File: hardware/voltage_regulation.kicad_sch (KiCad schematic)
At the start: 33 parts, among them U4 TPS51388VABR, U5 LD39050PU33R

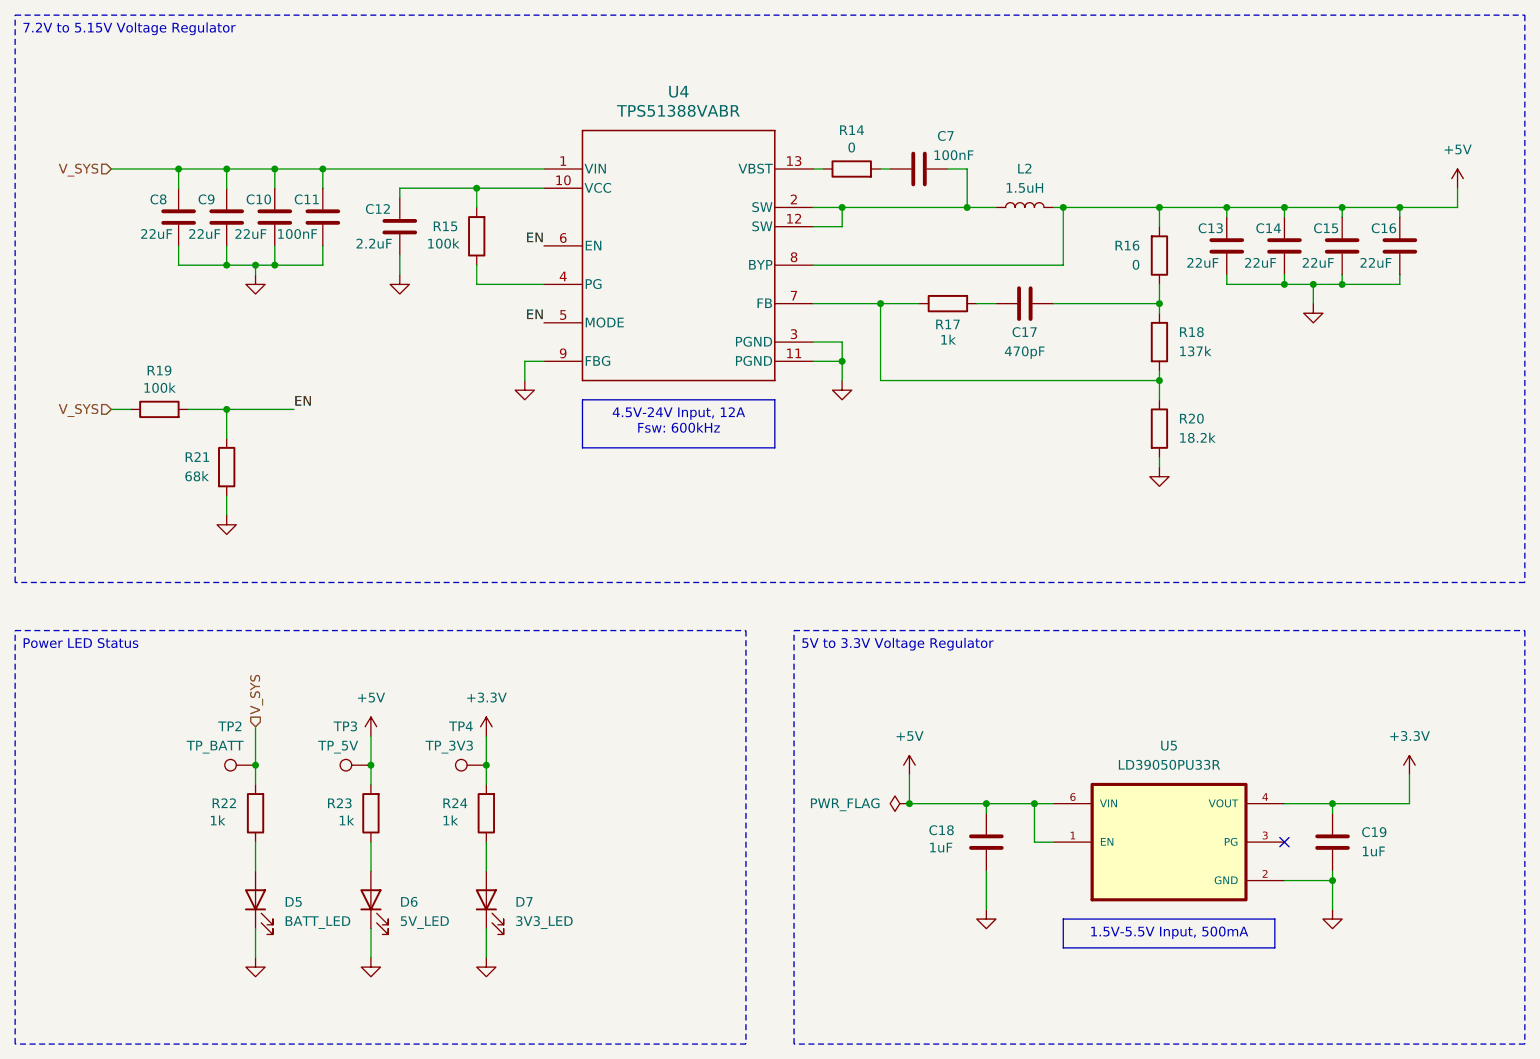
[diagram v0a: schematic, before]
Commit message: schematic update
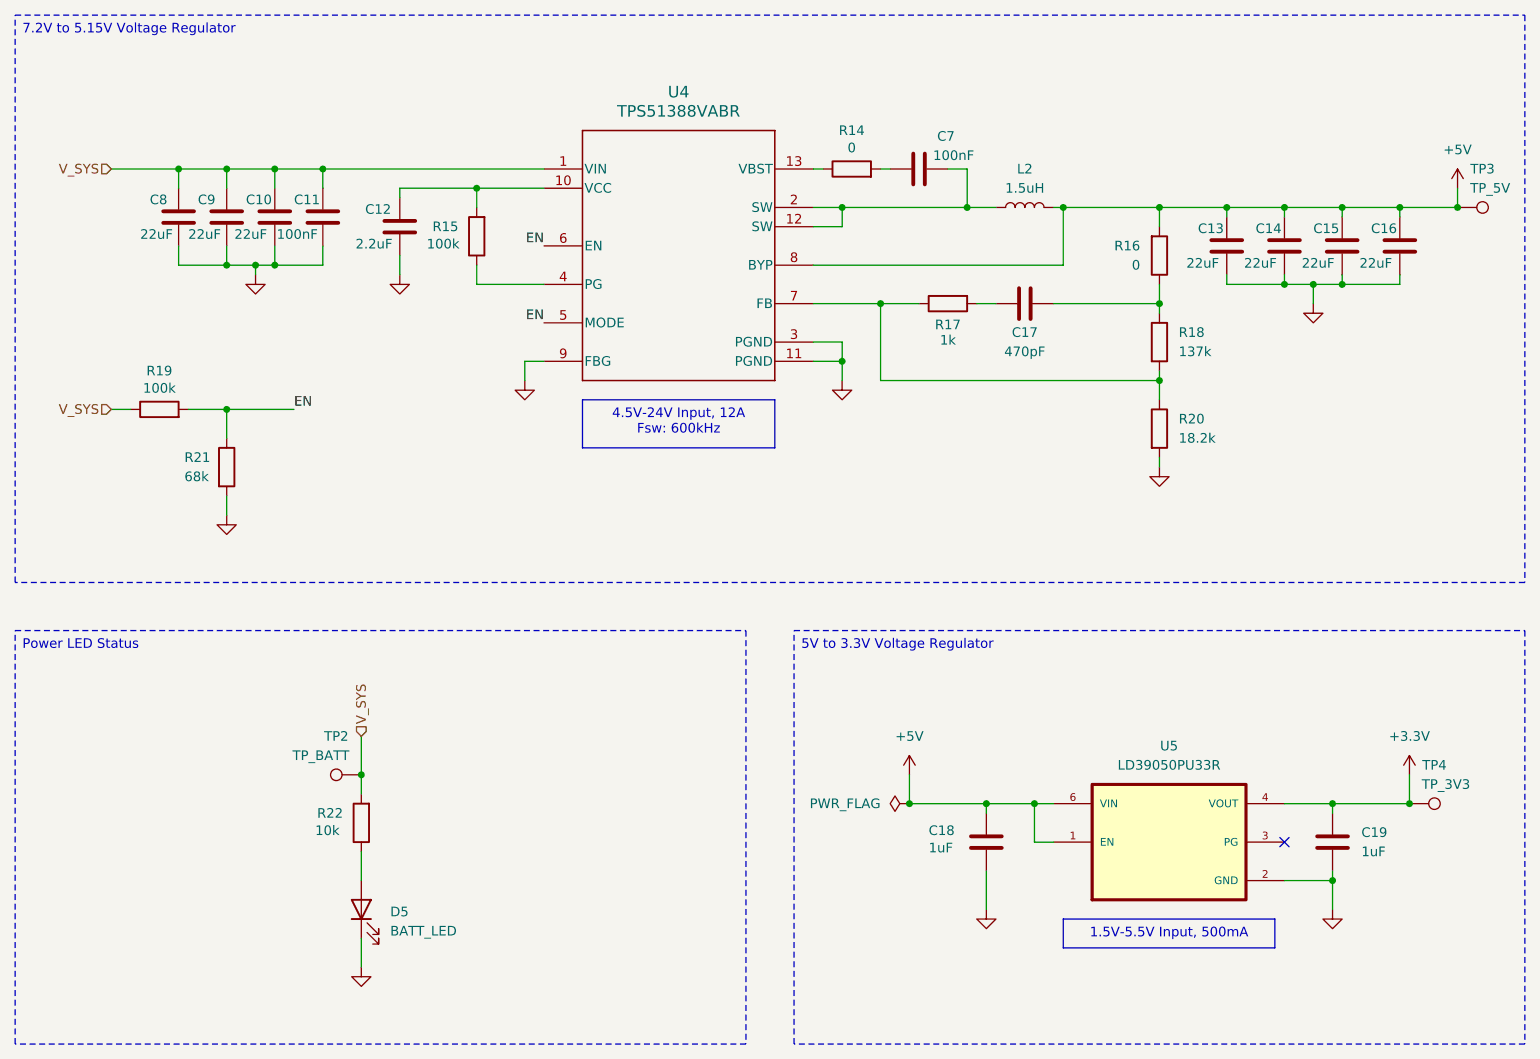
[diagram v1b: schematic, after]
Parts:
- removed D6: 5V_LED, LED_SMD:LED_0603_1608Metric, symbol Device:LED
- removed D7: 3V3_LED, LED_SMD:LED_0603_1608Metric, symbol Device:LED
- removed R23, R24: 1k, Resistor_SMD:R_0603_1608Metric, symbol Device:R
- D5: JLCPCB Part # C5478395 -> C6650185; MPN 150060SS55040 -> 150060BS55040
- R22: value 1k -> 10k; footprint Resistor_SMD:R_0603_1608Metric -> Resistor_SMD:R_0402_1005Metric; JLCPCB Part # (none) -> C191984
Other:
- moved on the sheet: D5, R22, TP2

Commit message: replacing components
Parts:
- D5: value BATT_LED -> 3V3 LED
- R22: value 10k -> 1k; JLCPCB Part # C191984 -> C844135
- renumbered TP3 to TP2, TP2 to TP3
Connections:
- net +3.3V: now also R22.2, TP3.1
- net V_SYS: no longer R22.2, TP3.1
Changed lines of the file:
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@@
 	(hierarchical_label "V_SYS"
 		(shape input)
-		(at 95.25 118.11 90)
-		(effects
-			(font
-				(size 1.27 1.27)
-			)
-			(justify left)
-		)
-	)
-	(hierarchical_label "V_SYS"
-		(shape input)
 		(at 62.23 43.18 180)
 		(effects
@@
 		(dnp no)
 		(fields_autoplaced yes)
-		(property "Reference" "#PWR030"
+		(property "Reference" "#PWR028"
 			(at 95.25 154.94 0)
 			(hide yes)
@@
 			(project "chromapi_motherboard_v1"
 				(path "/d1a31f26-03e0-43e1-89c1-031fe31befc5/19a2634a-eca3-4c2c-b35f-9c69362f2888"
-					(reference "#PWR030")
+					(reference "#PWR028")
 					(unit 1)
 				)
@@
 		(dnp no)
 		(fields_autoplaced yes)
-		(property "Reference" "#PWR028"
+		(property "Reference" "#PWR026"
 			(at 177.8 147.32 0)
 			(hide yes)
@@
 			(project "chromapi_motherboard_v1"
 				(path "/d1a31f26-03e0-43e1-89c1-031fe31befc5/19a2634a-eca3-4c2c-b35f-9c69362f2888"
-					(reference "#PWR028")
+					(reference "#PWR026")
 					(unit 1)
 				)
@@
 		(dnp no)
 		(fields_autoplaced yes)
-		(property "Reference" "#PWR029"
+		(property "Reference" "#PWR027"
 			(at 223.52 147.32 0)
 			(hide yes)
@@
 			(project "chromapi_motherboard_v1"
 				(path "/d1a31f26-03e0-43e1-89c1-031fe31befc5/19a2634a-eca3-4c2c-b35f-9c69362f2888"
-					(reference "#PWR029")
+					(reference "#PWR027")
 					(unit 1)
 				)
@@
 			)
 		)
-		(property "Value" "10k"
+		(property "Value" "1k"
 			(at 89.154 130.556 0)
 			(show_name no)
@@
 			)
 		)
-		(property "JLCPCB Part #" "C191984"
+		(property "JLCPCB Part #" "C844135"
 			(at 95.25 129.54 0)
 			(hide yes)
@@
 	)
 	(symbol
+		(lib_id "power:+3.3V")
+		(at 95.25 118.11 0)
+		(unit 1)
+		(body_style 1)
+		(exclude_from_sim no)
+		(in_bom yes)
+		(on_board yes)
+		(in_pos_files yes)
+		(dnp no)
+		(fields_autoplaced yes)
+		(property "Reference" "#PWR0112"
+			(at 95.25 121.92 0)
+			(hide yes)
+			(show_name no)
+			(do_not_autoplace no)
+			(effects
+				(font
+					(size 1.27 1.27)
+				)
+			)
+		)
+		(property "Value" "+3.3V"
+			(at 95.25 113.03 0)
+			(show_name no)
+			(do_not_autoplace no)
+			(effects
+				(font
+					(size 1.27 1.27)
+				)
+			)
+		)
+		(property "Footprint" ""
+			(at 95.25 118.11 0)
+			(hide yes)
+			(show_name no)
+			(do_not_autoplace no)
+			(effects
+				(font
+					(size 1.27 1.27)
+				)
+			)
+		)
+		(property "Datasheet" ""
+			(at 95.25 118.11 0)
+			(hide yes)
+			(show_name no)
+			(do_not_autoplace no)
+			(effects
+				(font
+					(size 1.27 1.27)
+				)
+			)
+		)
+		(property "Description" "Power symbol creates a global label with name \"+3.3V\""
+			(at 95.25 118.11 0)
+			(hide yes)
+			(show_name no)
+			(do_not_autoplace no)
+			(effects
+				(font
+					(size 1.27 1.27)
+				)
+			)
+		)
+		(pin "1"
+		)
+		(instances
+			(project "chromapi_motherboard_v1"
+				(path "/d1a31f26-03e0-43e1-89c1-031fe31befc5/19a2634a-eca3-4c2c-b35f-9c69362f2888"
+					(reference "#PWR0112")
+					(unit 1)
+				)
+			)
+		)
+	)
+	(symbol
 		(lib_id "Device:R")
 		(at 200.66 54.61 0)
@@
 		(in_pos_files yes)
 		(dnp no)
-		(property "Reference" "TP2"
+		(property "Reference" "TP3"
 			(at 91.948 118.11 90)
 			(show_name no)
@@
 			(project "chromapi_motherboard_v1"
 				(path "/d1a31f26-03e0-43e1-89c1-031fe31befc5/19a2634a-eca3-4c2c-b35f-9c69362f2888"
-					(reference "TP2")
+					(reference "TP3")
 					(unit 1)
 				)
@@
 		(dnp no)
 		(fields_autoplaced yes)
-		(property "Reference" "#PWR027"
+		(property "Reference" "#PWR025"
 			(at 233.68 127 0)
 			(hide yes)
@@
 			(project "chromapi_motherboard_v1"
 				(path "/d1a31f26-03e0-43e1-89c1-031fe31befc5/19a2634a-eca3-4c2c-b35f-9c69362f2888"
-					(reference "#PWR027")
+					(reference "#PWR025")
 					(unit 1)
 				)
@@
 		(in_pos_files yes)
 		(dnp no)
-		(property "Reference" "TP3"
+		(property "Reference" "TP2"
 			(at 243.332 43.18 90)
 			(show_name no)
@@
 			(project "chromapi_motherboard_v1"
 				(path "/d1a31f26-03e0-43e1-89c1-031fe31befc5/19a2634a-eca3-4c2c-b35f-9c69362f2888"
-					(reference "TP3")
+					(reference "TP2")
 					(unit 1)
 				)
@@
 		(dnp no)
 		(fields_autoplaced yes)
-		(property "Reference" "#PWR026"
+		(property "Reference" "#PWR024"
 			(at 167.64 127 0)
 			(hide yes)
@@
 			(project "chromapi_motherboard_v1"
 				(path "/d1a31f26-03e0-43e1-89c1-031fe31befc5/19a2634a-eca3-4c2c-b35f-9c69362f2888"
-					(reference "#PWR026")
+					(reference "#PWR024")
 					(unit 1)
 				)
@@
 			)
 		)
-		(property "Value" "BATT_LED"
+		(property "Value" "3V3 LED"
 			(at 99.06 143.8274 90)
 			(show_name no)

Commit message: schematic update
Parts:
- removed TP3: TP_BATT, TestPoint:TestPoint_Pad_D1.5mm, symbol Connector:TestPoint
- added TP2: TP_BATT, TestPoint:TestPoint_Pad_D1.5mm, symbol Connector:TestPoint
- renumbered TP2 to TP1, TP4 to TP3
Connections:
- net V_SYS: now also TP2.1

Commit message: update schematic
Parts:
- U5: PACKAGE DFN-6 STMicroelectronics -> (none)
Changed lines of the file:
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@@
 			)
 		)
-		(property "Manufacturer" ""
+		(property "MANUFACTURER" ""
 			(at 233.68 127 90)
 			(hide yes)
@@
 			)
 		)
-		(property "Manufacturer" ""
+		(property "MANUFACTURER" ""
 			(at 83.82 49.53 0)
 			(hide yes)
@@
 			)
 		)
-		(property "Manufacturer" ""
+		(property "MANUFACTURER" ""
 			(at 68.58 74.93 90)
 			(hide yes)
@@
 			)
 		)
-		(property "Manufacturer" ""
+		(property "MANUFACTURER" ""
 			(at 77.47 82.55 0)
 			(hide yes)
@@
 			)
 		)
-		(property "Manufacturer" ""
+		(property "MANUFACTURER" ""
 			(at 182.88 60.96 90)
 			(hide yes)
@@
 			)
 		)
-		(property "Manufacturer" ""
+		(property "MANUFACTURER" ""
 			(at 95.25 129.54 0)
 			(hide yes)
@@
 			)
 		)
-		(property "PACKAGE" "DFN-6 STMicroelectronics"
+		(property "Package" "DFN-6 STMicroelectronics"
 			(at 201.93 132.08 0)
 			(hide yes)
@@
 			)
 		)
-		(property "Manufacturer" ""
+		(property "MANUFACTURER" ""
 			(at 209.55 53.34 0)
 			(hide yes)
@@
 			)
 		)
-		(property "Manufacturer" ""
+		(property "MANUFACTURER" ""
 			(at 200.66 77.47 0)
 			(hide yes)
@@
 			)
 		)
-		(property "Manufacturer" ""
+		(property "MANUFACTURER" ""
 			(at 177.8 132.08 0)
 			(hide yes)
@@
 			)
 		)
-		(property "Manufacturer" ""
+		(property "MANUFACTURER" ""
 			(at 200.66 54.61 0)
 			(hide yes)
@@
 			)
 		)
-		(property "Manufacturer" ""
+		(property "MANUFACTURER" ""
 			(at 160.02 43.18 90)
 			(hide yes)
@@
 			)
 		)
-		(property "Manufacturer" ""
+		(property "MANUFACTURER" ""
 			(at 110.49 52.07 0)
 			(hide yes)
@@
 			)
 		)
-		(property "Manufacturer" ""
+		(property "MANUFACTURER" ""
 			(at 77.47 49.53 0)
 			(hide yes)
@@
 			)
 		)
-		(property "Manufacturer" ""
+		(property "MANUFACTURER" ""
 			(at 200.66 66.04 0)
 			(hide yes)
@@
 			)
 		)
-		(property "Manufacturer" ""
+		(property "MANUFACTURER" ""
 			(at 223.52 132.08 0)
 			(hide yes)
@@
 			)
 		)
-		(property "Manufacturer" ""
+		(property "MANUFACTURER" ""
 			(at 217.17 53.34 0)
 			(hide yes)
@@
 			)
 		)
-		(property "Manufacturer" ""
+		(property "MANUFACTURER" ""
 			(at 90.17 49.53 0)
 			(hide yes)
@@
 			)
 		)
-		(property "Manufacturer" ""
+		(property "MANUFACTURER" ""
 			(at 240.03 48.26 90)
 			(hide yes)
@@
 			)
 		)
-		(property "Manufacturer" ""
+		(property "MANUFACTURER" ""
 			(at 232.41 53.34 0)
 			(hide yes)
@@
 			)
 		)
-		(property "Manufacturer" ""
+		(property "MANUFACTURER" ""
 			(at 168.91 43.18 90)
 			(hide yes)
@@
 			)
 		)
-		(property "Manufacturer" ""
+		(property "MANUFACTURER" ""
 			(at 64.77 74.93 90)
 			(hide yes)
@@
 			)
 		)
-		(property "Manufacturer" ""
+		(property "MANUFACTURER" ""
 			(at 172.72 60.96 90)
 			(hide yes)
@@
 			)
 		)
-		(property "Manufacturer" ""
+		(property "MANUFACTURER" ""
 			(at 71.12 49.53 0)
 			(hide yes)
@@
 			)
 		)
-		(property "Manufacturer" ""
+		(property "MANUFACTURER" ""
 			(at 100.33 50.8 0)
 			(hide yes)
@@
 			)
 		)
-		(property "Manufacturer" ""
+		(property "MANUFACTURER" ""
 			(at 224.79 53.34 0)
 			(hide yes)
